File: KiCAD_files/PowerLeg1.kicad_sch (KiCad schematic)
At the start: 72 parts, among them Q301 IPD200N15N3, Q302 IPD200N15N3, Q303 IPD200N15N3, U301 AMC1100DUB, U302 ACS730xLCTR-20AB, U303 UCC21222DR, U304 OPA316, U305 OPA316, U306 SFH617A-2X009T

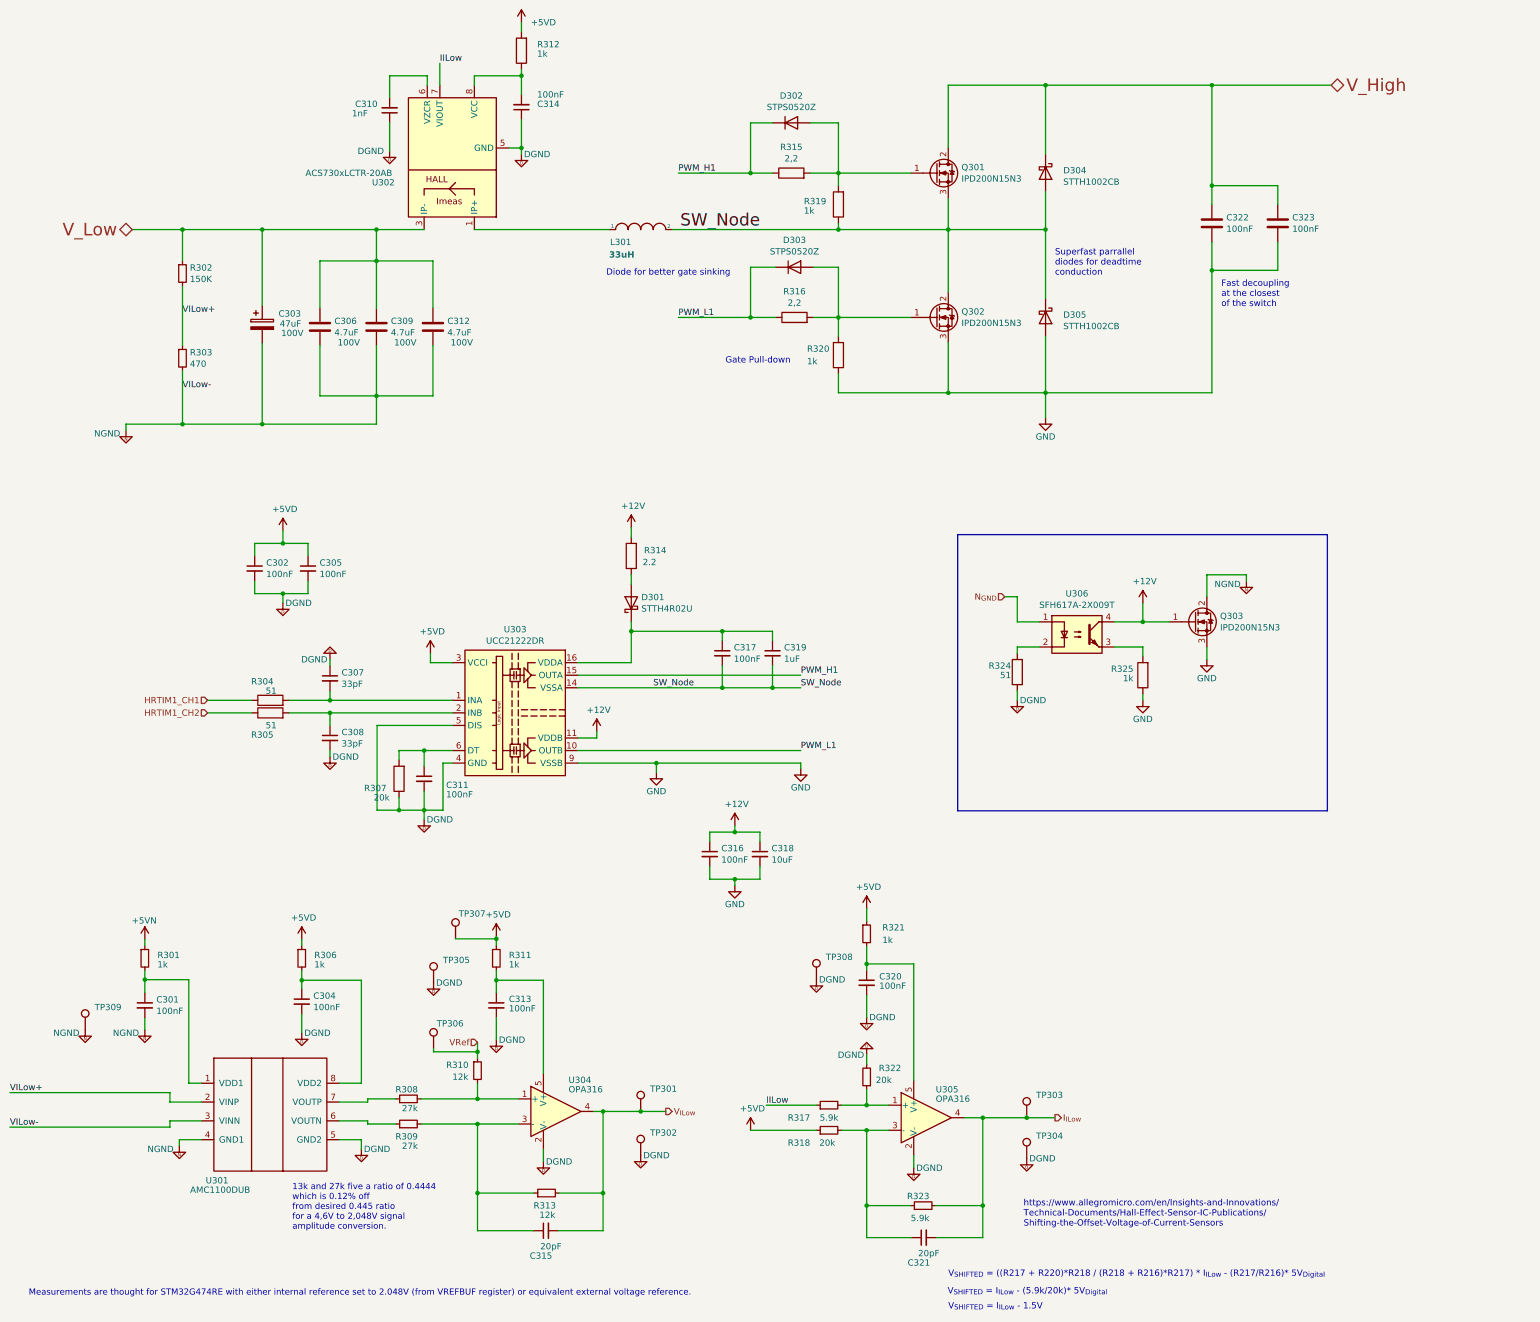
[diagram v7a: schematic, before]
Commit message: WIP: added features for the RJ45 communication link. Added fast RS485 Added HRTIM Sync Added current share analog bus Added external VREF Added dedicated supply power supply pins for the data manager
Former-commit-id: 7d7dbd6688aaf47caa2ea5f91bf9cef552f6a24c
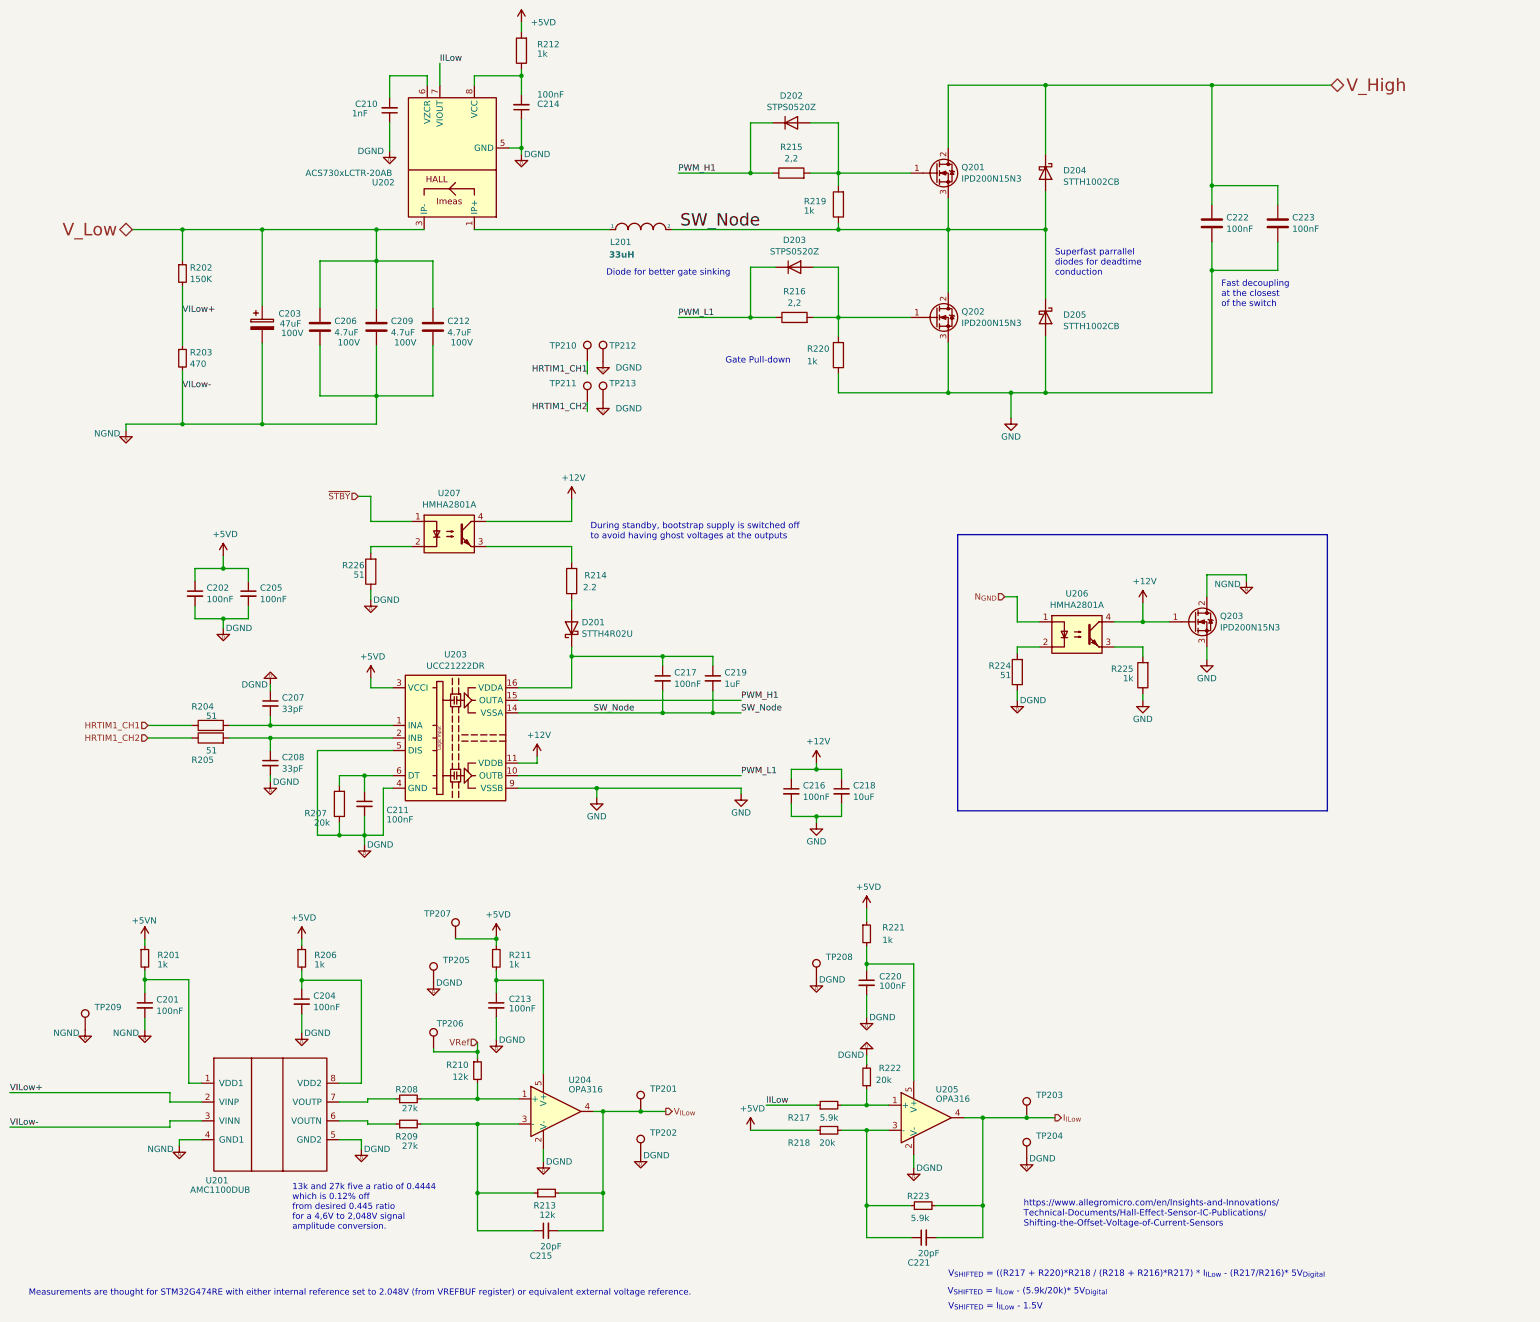
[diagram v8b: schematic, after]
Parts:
- added R226: 51, Footprints:R_0805_2012Metric, symbol Device:R
- added TP210, TP211, TP212, TP213: TestPoint, Footprints:TestPoint_THTPad_D1.5mm_Drill0.7mm, symbol Connector:TestPoint
- added U207: HMHA2801A, Package_SO:SO-4_4.4x2.3mm_P1.27mm, symbol Isolator:SFH617A-2X009T
- TP201: renamed from TP301; footprint TestPoint:TestPoint_Pad_D1.0mm -> Footprints:TestPoint_THTPad_D1.5mm_Drill0.7mm
- TP202: renamed from TP302; footprint TestPoint:TestPoint_Pad_D1.0mm -> Footprints:TestPoint_THTPad_D1.5mm_Drill0.7mm
- TP203: renamed from TP303; footprint TestPoint:TestPoint_Pad_D1.0mm -> Footprints:TestPoint_THTPad_D1.5mm_Drill0.7mm
- TP204: renamed from TP304; footprint TestPoint:TestPoint_Pad_D1.0mm -> Footprints:TestPoint_THTPad_D1.5mm_Drill0.7mm
- TP205: renamed from TP305; footprint TestPoint:TestPoint_Pad_D1.0mm -> Footprints:TestPoint_THTPad_D1.5mm_Drill0.7mm
- TP206: renamed from TP306; footprint TestPoint:TestPoint_Pad_D1.0mm -> Footprints:TestPoint_THTPad_D1.5mm_Drill0.7mm
- TP207: renamed from TP307; footprint TestPoint:TestPoint_Pad_D1.0mm -> Footprints:TestPoint_THTPad_D1.5mm_Drill0.7mm
- TP208: renamed from TP308; footprint TestPoint:TestPoint_Pad_D1.0mm -> Footprints:TestPoint_THTPad_D1.5mm_Drill0.7mm
- TP209: renamed from TP309; footprint TestPoint:TestPoint_Pad_D1.0mm -> Footprints:TestPoint_THTPad_D1.5mm_Drill0.7mm
- U206: renamed from U306; value SFH617A-2X009T -> HMHA2801A; footprint Package_DIP:SMDIP-4_W7.62mm -> Package_SO:SO-4_4.4x2.3mm_P1.27mm
- renumbered C301 to C201, C302 to C202, C303 to C203, C304 to C204, C305 to C205, C306 to C206, C307 to C207, C308 to C208, C309 to C209, C310 to C210, C311 to C211, C312 to C212, C313 to C213, C314 to C214, C315 to C215, C316 to C216, C317 to C217, C318 to C218, C319 to C219, C320 to C220, C321 to C221, C322 to C222, C323 to C223, D301 to D201, D302 to D202, D303 to D203, D304 to D204, D305 to D205, L301 to L201, Q301 to Q201, Q302 to Q202, Q303 to Q203, R301 to R201, R302 to R202, R303 to R203, R304 to R204, R305 to R205, R306 to R206, R307 to R207, R308 to R208, R309 to R209, R310 to R210, R311 to R211, R312 to R212, R313 to R213, R314 to R214, R315 to R215, R316 to R216, R317 to R217, R318 to R218, R319 to R219, R320 to R220, R321 to R221, R322 to R222, R323 to R223, R324 to R224, R325 to R225, U301 to U201, U302 to U202, U303 to U203, U304 to U204, U305 to U205
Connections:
- net +12V: now also U207.4; no longer R214.2
- net DGND: now also R226.1, TP212.1, TP213.1
- net HRTIM1_CH1: now also TP210.1
- net HRTIM1_CH2: now also TP211.1
- new net: R226.2, U207.2
- new net: R214.2, U207.3
- new net ~{STBY}: U207.1
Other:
- note added: "During standby, bootstrap supply is switched off to avoid having ghost voltages at the outputs"
- moved on the sheet: C202, C205, C207, C208, C211, C216, C217, C218, C219, D201, R204, R205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
